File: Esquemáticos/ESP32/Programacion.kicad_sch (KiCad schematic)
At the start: 13 parts, among them J4 USB Programador, U7 ESP32-WROOM-32

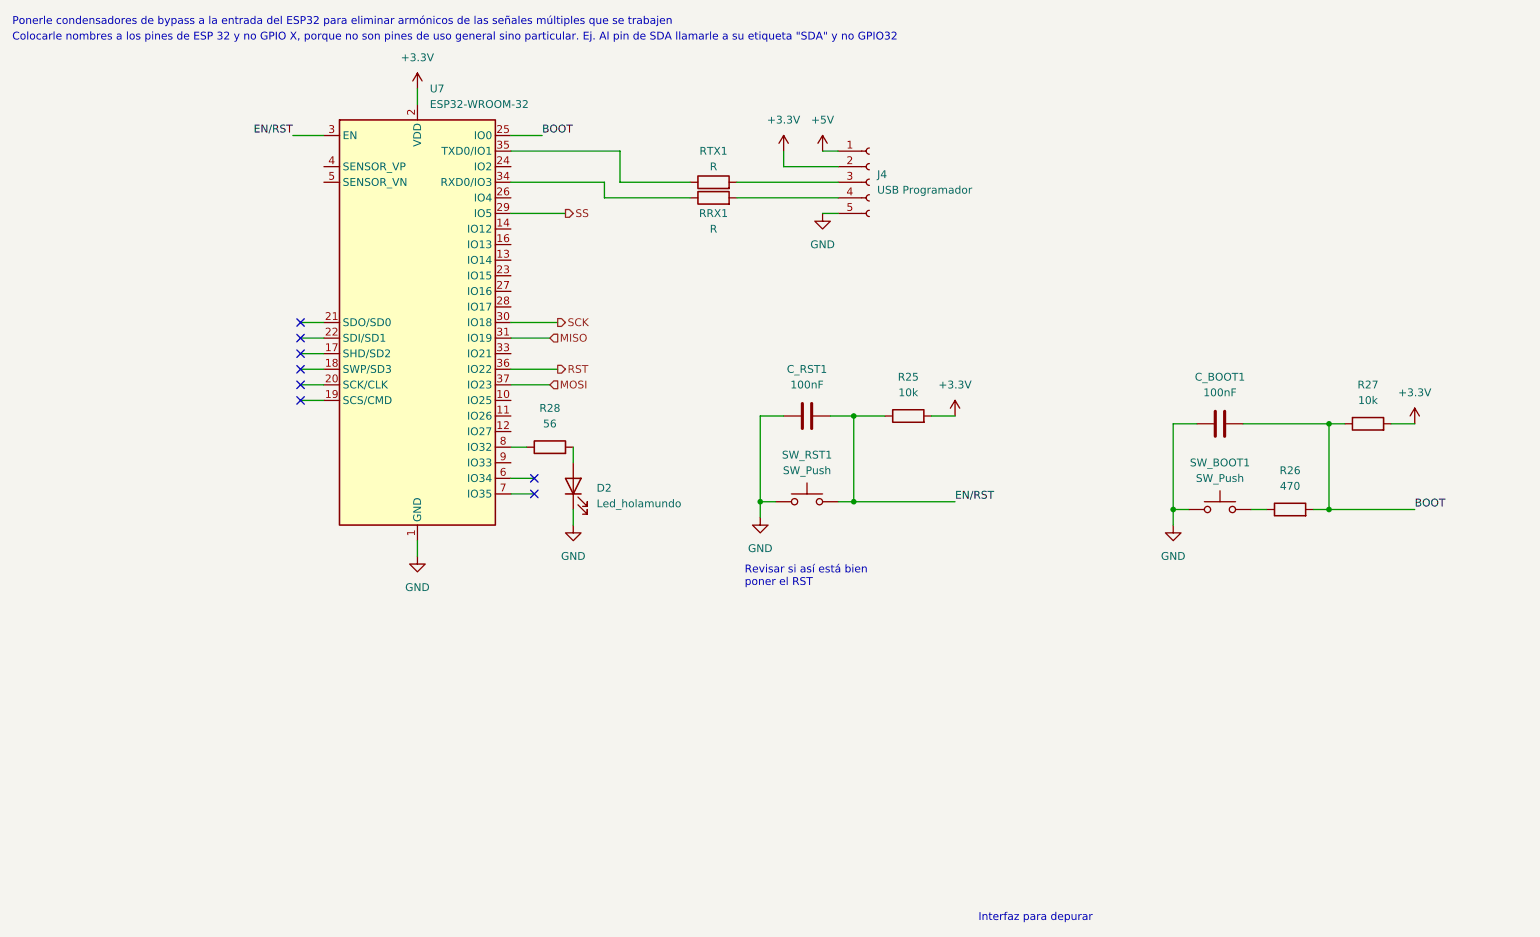
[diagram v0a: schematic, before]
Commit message: PCB versión 1 (Faltan zonas de GND)
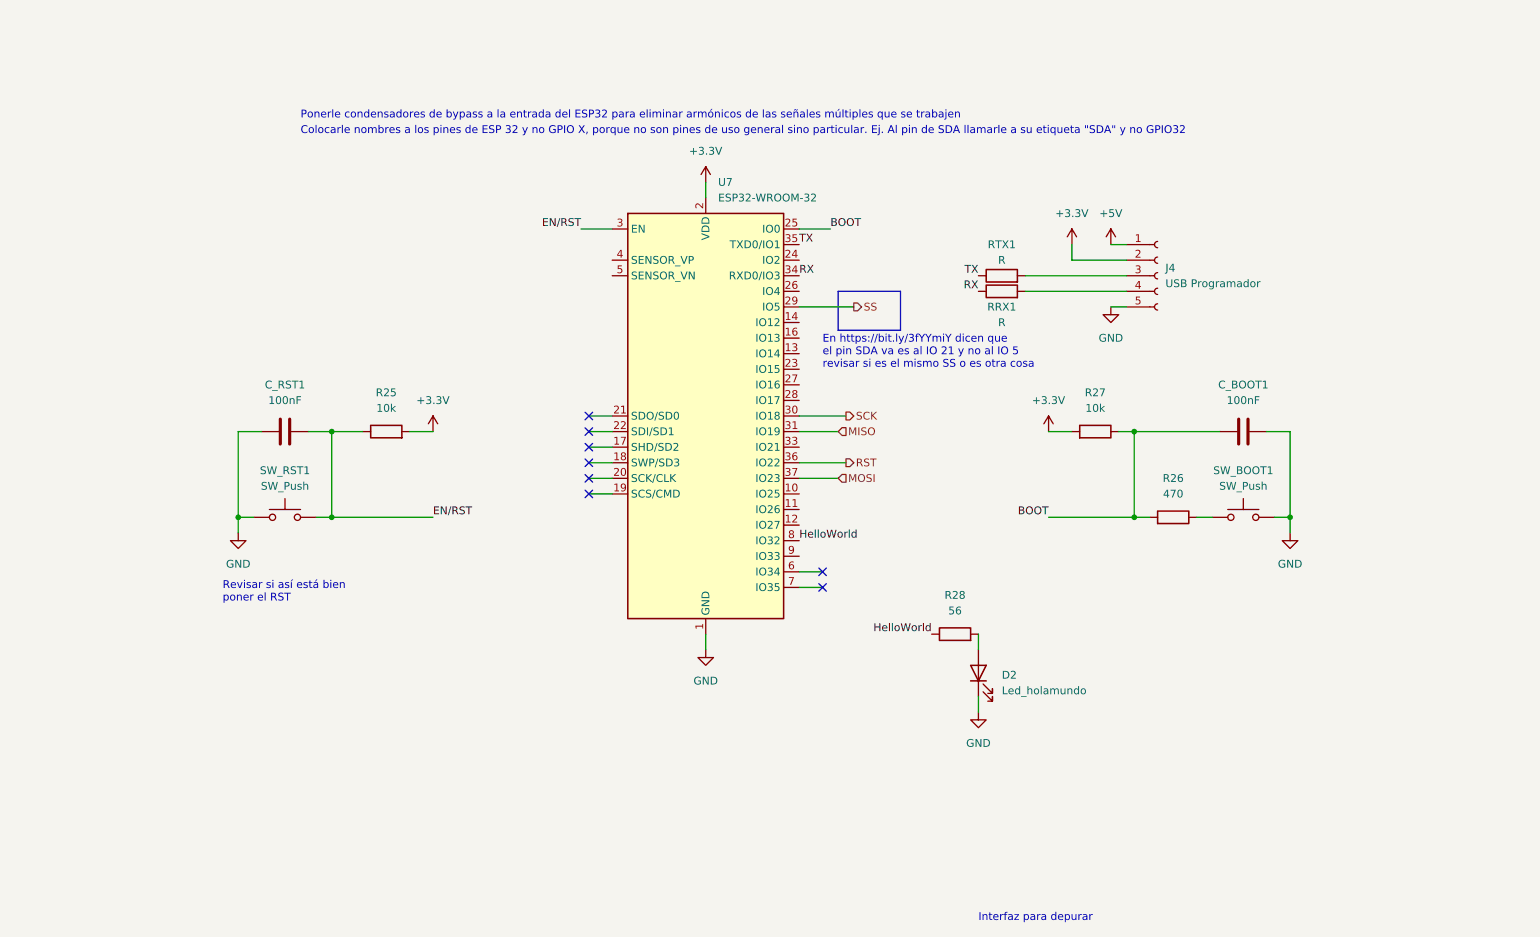
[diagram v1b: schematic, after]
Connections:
- net RX: now reaches RRX1.1, U7.34 (RXD0/IO3)
- net TX: now reaches RTX1.1, U7.35 (TXD0/IO1)
- net HelloWorld: now reaches R28.1, U7.8 (IO32)
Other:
- note added: "En https://bit.ly/3fYYmiY dicen que el pin SDA va es al IO 21 y no al IO 5 revisar si es el mismo SS o es otra cosa"
- moved on the sheet: C_BOOT1, C_RST1, D2, J4, R25, R26, R27, R28, RRX1, RTX1, SW_BOOT1, SW_RST1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

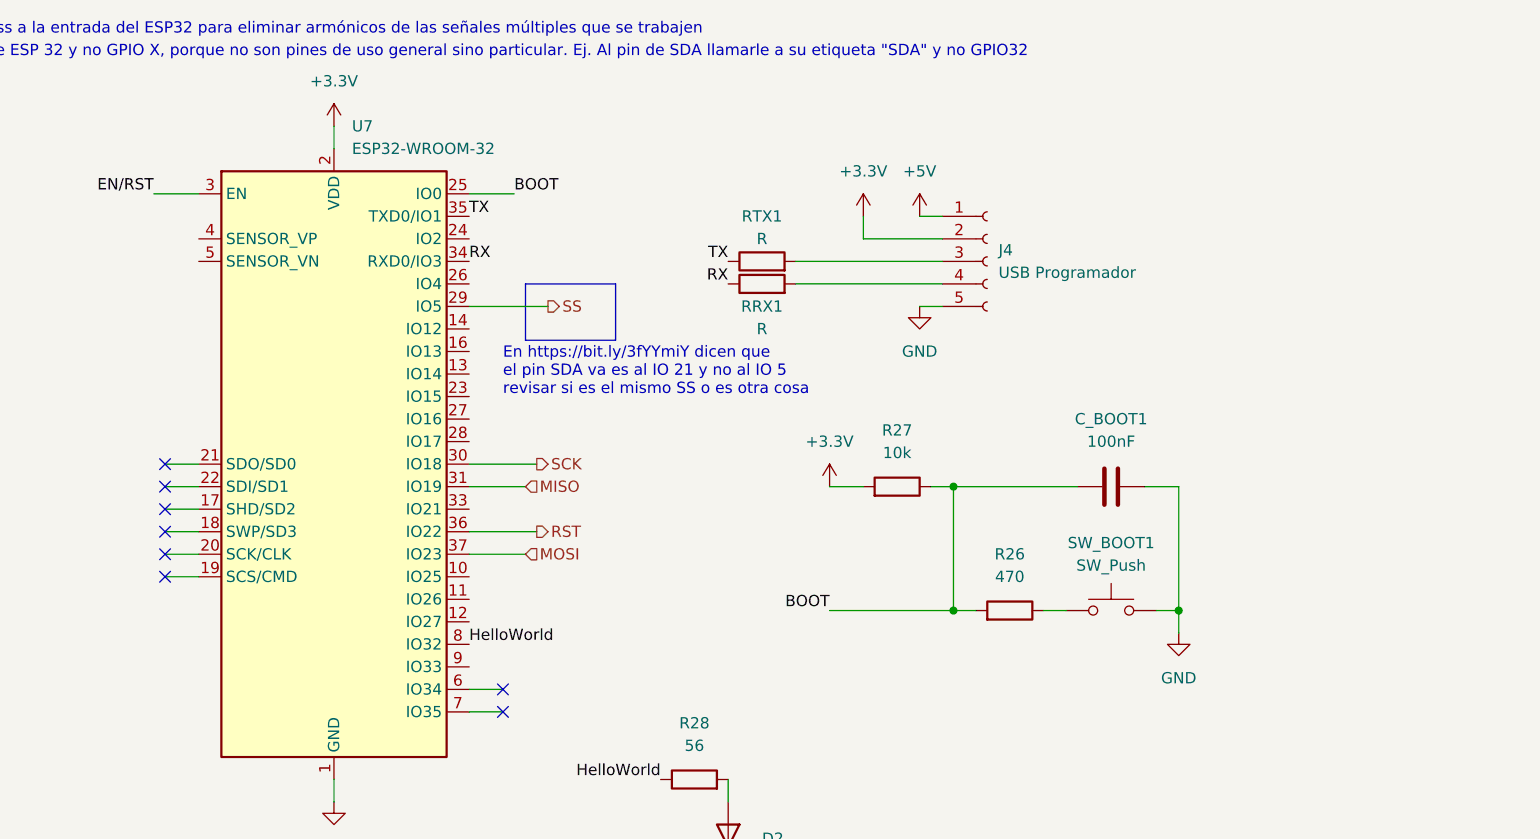
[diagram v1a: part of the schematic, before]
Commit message: Añadí las conexiones con los optoacopladores
Además arreglé la posición de algunas vías.
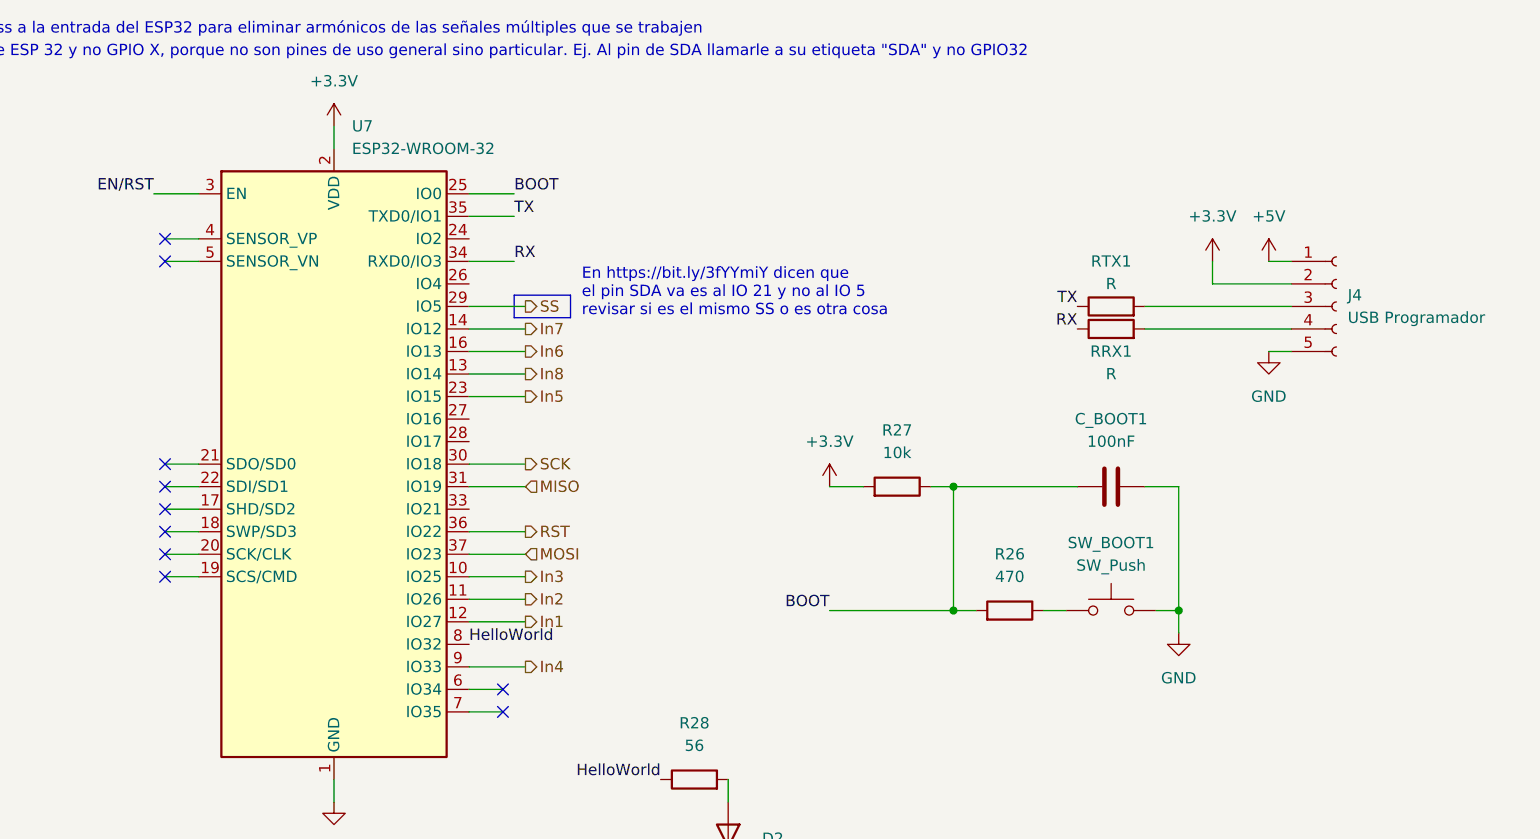
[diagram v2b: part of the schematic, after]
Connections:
- net In3: now reaches U7.10 (IO25)
- net In2: now reaches U7.11 (IO26)
- net In1: now reaches U7.12 (IO27)
- net In8: now reaches U7.13 (IO14)
- net In7: now reaches U7.14 (IO12)
- net In6: now reaches U7.16 (IO13)
- net In5: now reaches U7.23 (IO15)
- net In4: now reaches U7.9 (IO33)
- no-connect marks 8 -> 10
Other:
- moved on the sheet: J4, RRX1, RTX1

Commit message: PCB terminada (pendiente de aprobación)
:sunglasses: :sunglasses: :sunglasses:
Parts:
- J4: footprint Connector_PinHeader_1.27mm:PinHeader_1x05_P1.27mm_Vertical -> Connector_PinHeader_2.54mm:PinHeader_1x05_P2.54mm_Vertical
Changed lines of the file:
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@@
       (effects (font (size 1.27 1.27)) (justify left))
     )
-    (property "Footprint" "Connector_PinHeader_1.27mm:PinHeader_1x05_P1.27mm_Vertical" (id 2) (at 255.27 90.17 0)
+    (property "Footprint" "Connector_PinHeader_2.54mm:PinHeader_1x05_P2.54mm_Vertical" (id 2) (at 255.27 90.17 0)
       (effects (font (size 1.27 1.27)) hide)
     )

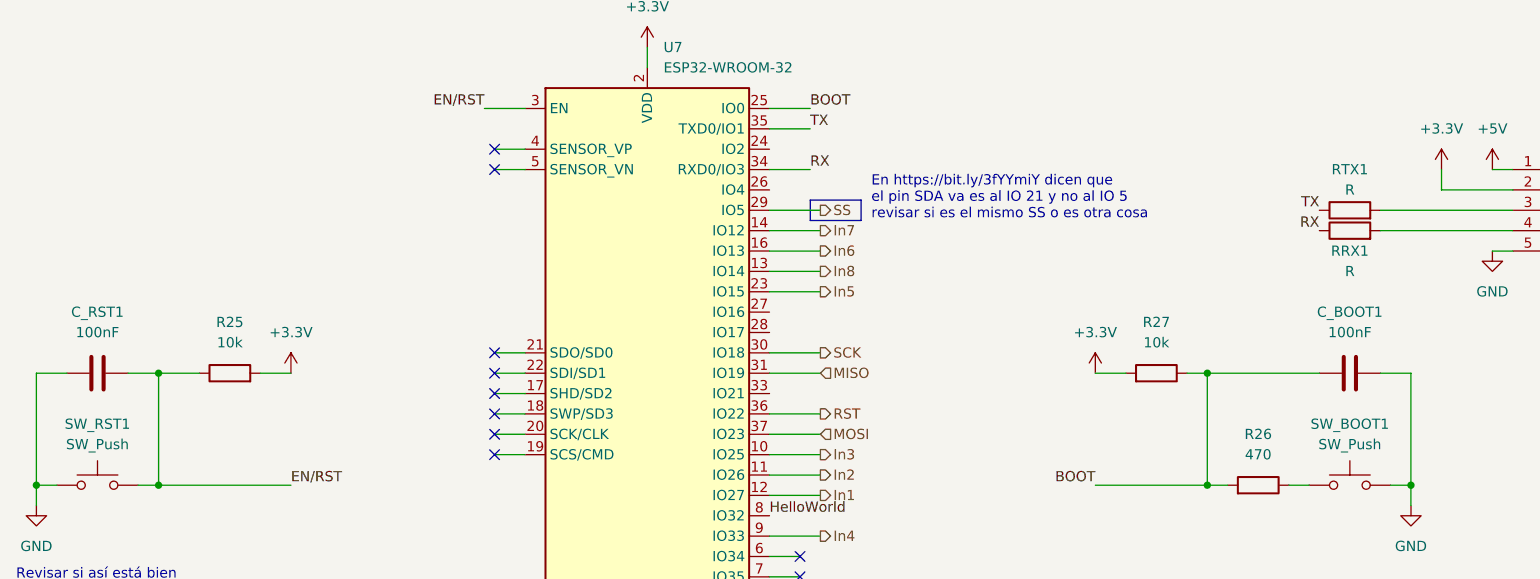
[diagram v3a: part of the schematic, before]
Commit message: Actualizada la PCB con impresiones de qué es cada pin de los conectores
Pendiente: Agregar capacitor de bypass en la entrada de 3v3 del ESP32 y listo, a comerciar con los chinos
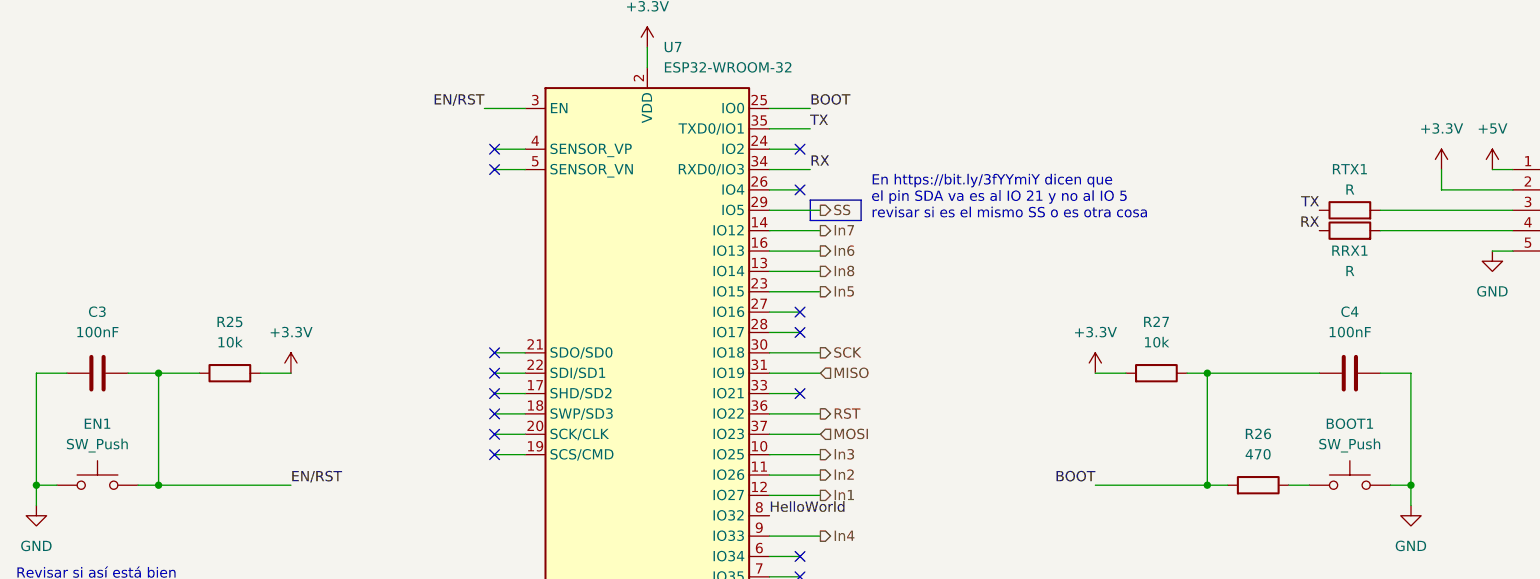
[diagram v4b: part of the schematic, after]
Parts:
- renumbered SW_BOOT1 to BOOT1, C_RST1 to C3, C_BOOT1 to C4, SW_RST1 to EN1
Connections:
- no-connect marks 10 -> 15
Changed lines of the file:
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@@
   )
   (no_connect (at 123.19 120.65))
+  (no_connect (at 161.29 113.03))
+  (no_connect (at 161.29 102.87))
+  (no_connect (at 161.29 87.63))
+  (no_connect (at 161.29 82.55))
+  (no_connect (at 161.29 105.41))
   (no_connect (at 123.19 107.95))
   (no_connect (at 123.19 82.55))
@@
     (stroke (width 0) (type default) (color 0 0 0 0))
   )
+  (wire (pts (xy 161.29 87.63) (xy 157.48 87.63))
+    (stroke (width 0) (type default) (color 0 0 0 0))
+  )
   (wire (pts (xy 161.29 133.35) (xy 157.48 133.35))
     (stroke (width 0) (type default) (color 0 0 0 0))
@@
     (stroke (width 0) (type default) (color 0 0 0 0))
   )
+  (wire (pts (xy 161.29 82.55) (xy 157.48 82.55))
+    (stroke (width 0) (type default) (color 0 0 0 0))
+  )
   (wire (pts (xy 81.28 110.49) (xy 81.28 124.46))
     (stroke (width 0) (type default) (color 0 0 0 0))
@@
     (stroke (width 0) (type default) (color 0 0 0 0))
   )
+  (wire (pts (xy 161.29 102.87) (xy 157.48 102.87))
+    (stroke (width 0) (type default) (color 0 0 0 0))
+  )
   (wire (pts (xy 237.49 124.46) (xy 237.49 110.49))
     (stroke (width 0) (type default) (color 0 0 0 0))
@@
     (stroke (width 0) (type default) (color 0 0 0 0))
   )
+  (wire (pts (xy 161.29 113.03) (xy 157.48 113.03))
+    (stroke (width 0) (type default) (color 0 0 0 0))
+  )
   (wire (pts (xy 186.69 153.67) (xy 186.69 156.21))
     (stroke (width 0) (type default) (color 0 0 0 0))
   )
   (wire (pts (xy 123.19 120.65) (xy 127 120.65))
+    (stroke (width 0) (type default) (color 0 0 0 0))
+  )
+  (wire (pts (xy 161.29 105.41) (xy 157.48 105.41))
     (stroke (width 0) (type default) (color 0 0 0 0))
   )
@@
   (symbol (lib_id "Switch:SW_Push") (at 229.87 124.46 0) (mirror y) (unit 1)
     (in_bom yes) (on_board yes) (fields_autoplaced)
-    (property "Reference" "SW_BOOT1" (id 0) (at 229.87 116.84 0))
+    (property "Reference" "BOOT1" (id 0) (at 229.87 116.84 0))
     (property "Value" "SW_Push" (id 1) (at 229.87 119.38 0))
     (property "Footprint" "Button_Switch_SMD:SW_SPST_TL3305A" (id 2) (at 229.87 119.38 0)
@@
   (symbol (lib_id "Switch:SW_Push") (at 73.66 124.46 0) (unit 1)
     (in_bom yes) (on_board yes) (fields_autoplaced)
-    (property "Reference" "SW_RST1" (id 0) (at 73.66 116.84 0))
+    (property "Reference" "EN1" (id 0) (at 73.66 116.84 0))
     (property "Value" "SW_Push" (id 1) (at 73.66 119.38 0))
     (property "Footprint" "Button_Switch_SMD:SW_SPST_TL3305A" (id 2) (at 73.66 119.38 0)
@@
   (symbol (lib_id "Device:C") (at 229.87 110.49 270) (mirror x) (unit 1)
     (in_bom yes) (on_board yes) (fields_autoplaced)
-    (property "Reference" "C_BOOT1" (id 0) (at 229.87 102.87 90))
+    (property "Reference" "C4" (id 0) (at 229.87 102.87 90))
     (property "Value" "100nF" (id 1) (at 229.87 105.41 90))
     (property "Footprint" "Capacitor_SMD:C_0603_1608Metric_Pad1.08x0.95mm_HandSolder" (id 2) (at 226.06 109.5248 0)
@@
   (symbol (lib_id "Device:C") (at 73.66 110.49 90) (unit 1)
     (in_bom yes) (on_board yes) (fields_autoplaced)
-    (property "Reference" "C_RST1" (id 0) (at 73.66 102.87 90))
+    (property "Reference" "C3" (id 0) (at 73.66 102.87 90))
     (property "Value" "100nF" (id 1) (at 73.66 105.41 90))
     (property "Footprint" "Capacitor_SMD:C_0603_1608Metric_Pad1.08x0.95mm_HandSolder" (id 2) (at 77.47 109.5248 0)
